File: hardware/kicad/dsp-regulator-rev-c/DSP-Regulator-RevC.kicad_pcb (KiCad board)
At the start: 2 copper layers, 291.9 x 100.9 mm, 218 parts, among them J1 1935161, J10 1935161, J11 1935161, J2 Wire con, J3 Wire con, J4 CLP-110-02-X-D, J5 CLP-110-02-X-D, J8 Conn_01x20_Pin, Q1 BSS138, Q10 PSMN5R2-60YL, Q11 PSMN5R2-60YL, Q12 PSMN5R2-60YL, Q2 BSS138, Q3 BSS138, Q4 BSS138, Q5 PSMN5R2-60YL, Q6 PSMN5R2-60YL, Q7 PSMN5R2-60YL, Q8 PSMN5R2-60YL, Q9 PSMN5R2-60YL, U1 LM2596S-ADJ, U10 INA2180A2IDGKR, U11 TLV1702AIDGKR, U12 TLV1702AIDGKR, U13 INA3221, U14 INA3221, U2 LM2596S-ADJ, U3 LM74502DDFR, U4 TLV9352, U5 TLV9352, U6 LM74502DDFR, U7 LM74502DDFR, U8 LM74502DDFR, U9 INA2180A2IDGKR

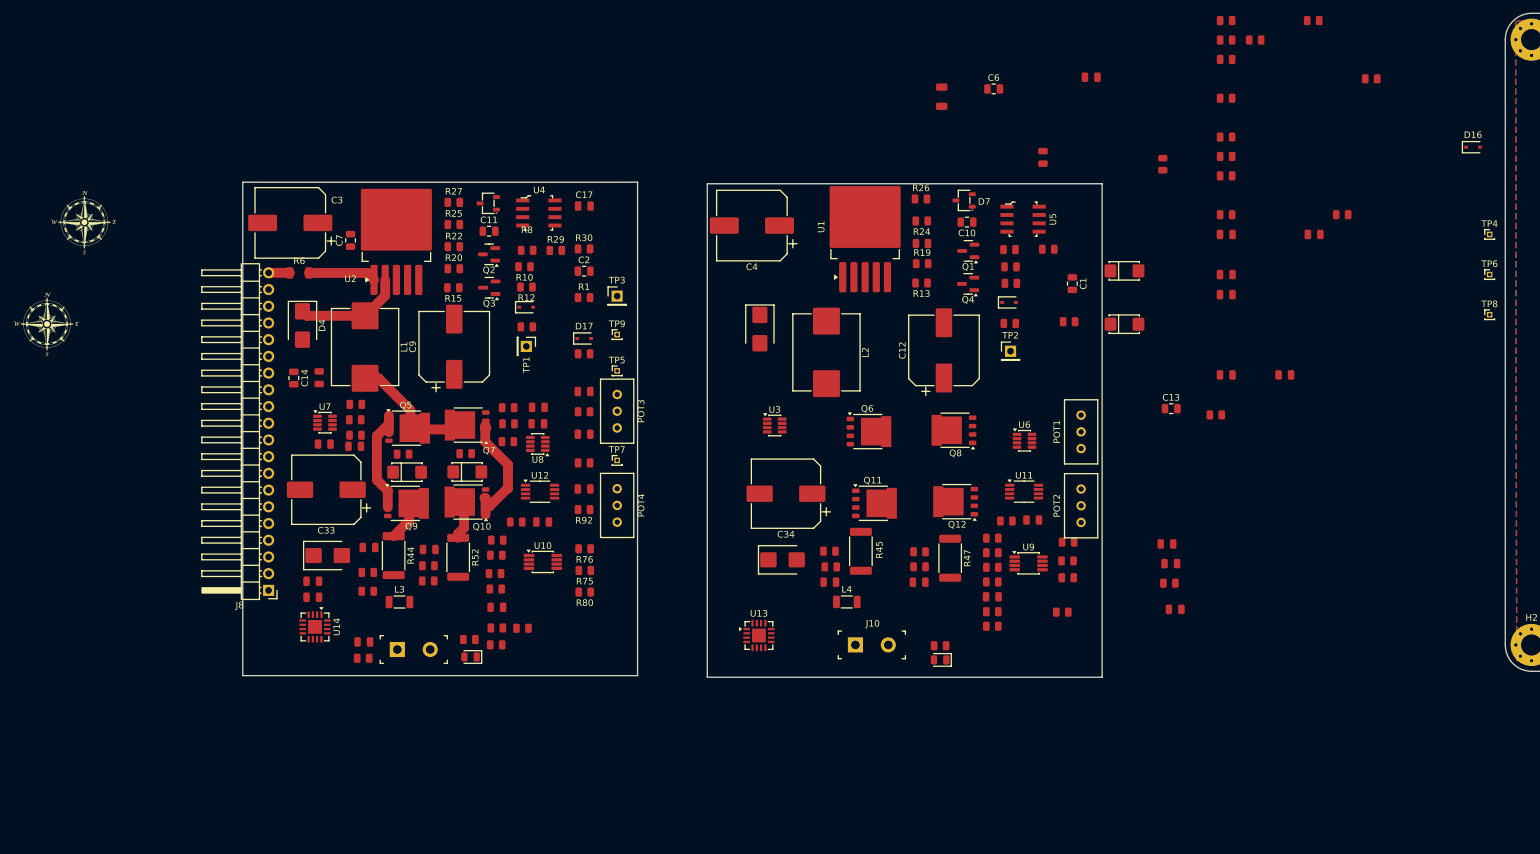
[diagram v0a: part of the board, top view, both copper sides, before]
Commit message: Save Rev-C regulator PCB routing progress
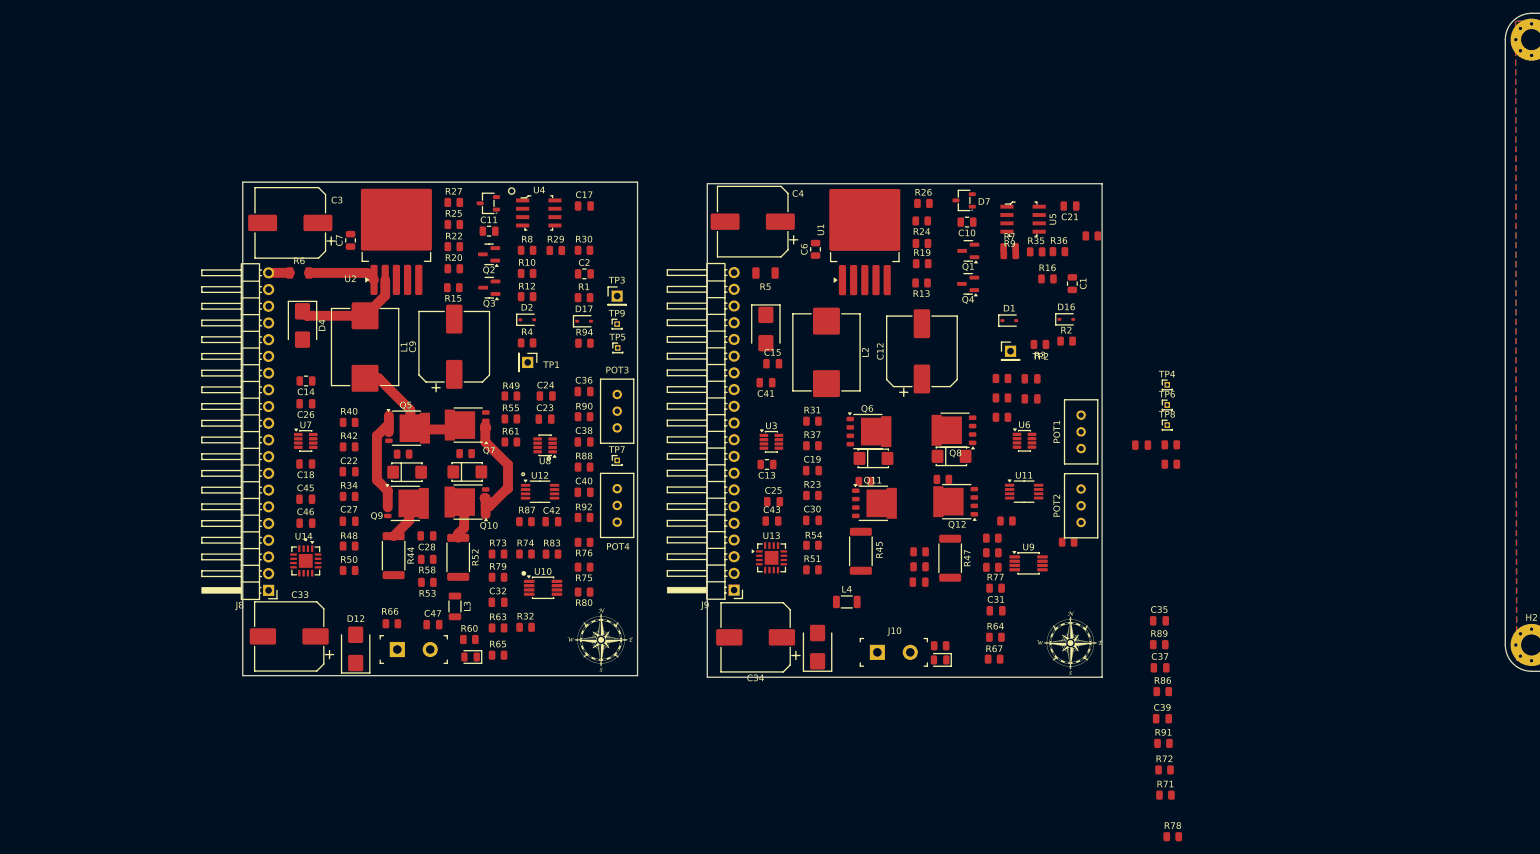
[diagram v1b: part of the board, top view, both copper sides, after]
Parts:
- added J9: Conn_01x20_Pin, Connector_PinHeader_2.54mm:PinHeader_1x20_P2.54mm_Horizontal, F.Cu at (18.3, 144.5)
- moved 10mm1 162.9 mm to (69.5, 152.5)
- moved 10mm2 96.9 mm to (-1.86, 152.0)
- moved R23 95.7 mm to (30.2, 130.1)
- moved R31 83.5 mm to (30.2, 118.8)
- moved R43 81.9 mm to (50.0, 127.7)
- moved C43 81.0 mm to (24.0, 134.0)
- moved R37 78.4 mm to (30.2, 122.6)
- moved C25 71.5 mm to (24.3, 131.1)
- moved R89 71.0 mm to (82.9, 152.8)
- moved C19 69.6 mm to (30.2, 126.3)
- moved R41 68.3 mm to (38.1, 128.0)
- moved R68 68.0 mm to (84.7, 122.4)
- moved D16 67.1 mm to (68.8, 103.3)
- moved R93 66.0 mm to (84.7, 125.4)
- moved C15 65.1 mm to (24.1, 110.1)
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
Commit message: Restore Rev-C regulator PCB updates
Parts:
- removed J10, J11: 1935161, digikey-footprints:Terminal_Block_D1.3mm_P5mm
- removed J8, J9: Conn_01x20_Pin, Connector_PinHeader_2.54mm:PinHeader_1x20_P2.54mm_Horizontal
- removed the TP3 at (233.5, 78.5)
- added C48: 100nF, PCM_JLCPCB:C_0805, F.Cu at (162.9, 160.1)
- added C49: 100nF, PCM_JLCPCB:C_0805, F.Cu at (189.7, 104.2)
- added C50: 1nF, PCM_JLCPCB:C_0805, F.Cu at (162.9, 163.1)
- added C51: 100nF, PCM_JLCPCB:C_0805, F.Cu at (189.7, 107.3)
- added C52: 100nF, PCM_JLCPCB:C_0805, F.Cu at (189.7, 110.3)
- added C53: 100nF, PCM_JLCPCB:C_0805, F.Cu at (189.7, 113.4)
- added D18: SS54B, PCM_JLCPCB:D_SMB, F.Cu at (110.8, 49.9)
- added D19: Yellow, PCM_JLCPCB:D_0805, F.Cu at (124.7, 59.2)
- added D20: 1N5819WS, Diode_SMD:D_SOD-323, F.Cu at (167.3, 163.1)
- added J6: Conn_01x03_Pin, Connector_PinHeader_2.54mm:PinHeader_1x03_P2.54mm_Vertical_SMD_Pin1Right, F.Cu at (158.5, 15.7)
- added J7: Conn_01x06_Pin, Connector_PinHeader_2.54mm:PinHeader_1x06_P2.54mm_Vertical_SMD_Pin1Right, F.Cu at (155.2, 50.6)
- added L5: 33uh, Inductor_SMD:L_Sunlord_MWSA1003S, F.Cu at (112.7, 59.0)
- added R100: 100kΩ, PCM_JLCPCB:R_0805, F.Cu at (185.2, 118.9)
- added R84: 10kΩ, PCM_JLCPCB:R_0805, F.Cu at (149.6, 165.7)
- added R95: 1kΩ, PCM_JLCPCB:R_0805, F.Cu at (158.4, 159.8)
- added R96: 390kΩ, PCM_JLCPCB:R_0805, F.Cu at (185.2, 107.1)
- added R97: 100kΩ, PCM_JLCPCB:R_0805, F.Cu at (185.2, 110.1)
- added R98: 10Ω, PCM_JLCPCB:R_0805, F.Cu at (185.2, 113.0)
- added R99: 390kΩ, PCM_JLCPCB:R_0805, F.Cu at (185.2, 116.0)
- added U15: LM74502DDFR, Package_TO_SOT_SMD:TSOT-23-8, F.Cu at (194.5, 105.1)
- added U16: LM74502DDFR, Package_TO_SOT_SMD:TSOT-23-8, F.Cu at (194.5, 109.7)
- C1: value 1nF -> 100nF; footprint Capacitor_SMD:C_0805_2012Metric -> PCM_JLCPCB:C_0805
- C10: value 100pF -> 10uF; footprint Capacitor_SMD:C_0805_2012Metric -> PCM_JLCPCB:C_0805
- C11: value 100pF -> 100nF; footprint Capacitor_SMD:C_0805_2012Metric -> PCM_JLCPCB:C_0805
- C12, C9: value 330uF 25v -> 100nF; footprint Capacitor_SMD:CP_Elec_10x10.5 -> PCM_JLCPCB:C_0805
- C13, C27, C42: value 100nF -> 1nF
- C14: value 100nF -> 100pF
- C17: value 100nF -> 470uf 50v; footprint PCM_JLCPCB:C_0805 -> Capacitor_SMD:CP_Elec_10x10.5
- C18, C20: footprint PCM_JLCPCB:C_0805 -> Capacitor_SMD:C_0805_2012Metric
- C19: value 100nF -> 330uF 25v; footprint PCM_JLCPCB:C_0805 -> Capacitor_SMD:CP_Elec_10x10.5
- C2: value 1nF -> 100pF
- C21, C23: value 100nF -> 10uF
- C22: value 100nF -> 470uf; footprint PCM_JLCPCB:C_0805 -> Capacitor_SMD:CP_Elec_10x10
- C25: value 10uF -> 1nF; footprint PCM_JLCPCB:C_0805 -> Capacitor_SMD:C_0805_2012Metric
- C26: value 10uF -> 100pF
- C28: value 100nF -> 100nf; footprint PCM_JLCPCB:C_0805 -> Capacitor_SMD:C_0805_2012Metric
- C29: value 100nF -> 1000uf 25v; footprint PCM_JLCPCB:C_0805 -> Capacitor_SMD:C_Elec_10x10.2
- C3: value 470uf 50v -> 100nF; footprint Capacitor_SMD:CP_Elec_10x10.5 -> PCM_JLCPCB:C_0805
- C30: value 100nF -> 470uf 25V; footprint PCM_JLCPCB:C_0805 -> Capacitor_SMD:CP_Elec_10x10.5
- C31: value 10uF -> 100nF
- C32: value 10uF -> 330uF 25v; footprint PCM_JLCPCB:C_0805 -> Capacitor_SMD:CP_Elec_10x10.5
- C33, C34: value 470uf -> 100nF; footprint Capacitor_SMD:CP_Elec_10x10 -> PCM_JLCPCB:C_0805
- C35, C36: value 1nF -> 100nF
- C38: value 1nF -> 100nF; footprint PCM_JLCPCB:C_0805 -> Capacitor_SMD:C_0805_2012Metric
- C5: value 100nf -> 100nF
- C6: value 100nF -> 470uf; footprint Capacitor_SMD:C_0805_2012Metric -> Capacitor_SMD:CP_Elec_10x10
- C7: value 100nF -> 10uF; footprint Capacitor_SMD:C_0805_2012Metric -> PCM_JLCPCB:C_0805
- C8: value 1000uf 25v -> 330uF 25v; footprint Capacitor_SMD:C_Elec_10x10.2 -> Capacitor_SMD:CP_Elec_10x10.5
- D1: value 1N5819WS -> BAT54C,215; footprint PCM_JLCPCB:D_SOD-323 -> PCM_JLCPCB:SOT-23-3_L2.9-W1.6-P1.90-LS2.8-BR
- D10: value 1SMA4742A -> SS54B; footprint PCM_JLCPCB:D_DO-214AC(SMA) -> PCM_JLCPCB:D_SMB
- D11: value 1SMA4742A -> SMBJ6.0CA; footprint PCM_JLCPCB:D_DO-214AC(SMA) -> PCM_JLCPCB:D_SMB
- D12: value SMBJ6.0CA -> Green; footprint PCM_JLCPCB:D_SMB -> PCM_JLCPCB:D_0805
- D13: value SMBJ6.0CA -> 1SMA4742A; footprint PCM_JLCPCB:D_SMB -> PCM_JLCPCB:D_DO-214AC(SMA)
- D14: value Green -> 1N5819WS; footprint PCM_JLCPCB:D_0805 -> PCM_JLCPCB:D_SOD-323
- D15: value Green -> Yellow
- D16: value 1N5819WS -> Red; footprint Diode_SMD:D_SOD-323 -> PCM_JLCPCB:D_0805
- D2: value 1N5819WS -> 1SMA4742A; footprint PCM_JLCPCB:D_SOD-323 -> PCM_JLCPCB:D_DO-214AC(SMA)
- D3: value Red -> SMBJ6.0CA; footprint PCM_JLCPCB:D_0805 -> PCM_JLCPCB:D_SMB
- D4: value SS54B -> Green; footprint PCM_JLCPCB:D_SMB -> PCM_JLCPCB:D_0805
- D6: value BAT54C,215 -> 1SMA4742A; footprint PCM_JLCPCB:SOT-23-3_L2.9-W1.6-P1.90-LS2.8-BR -> PCM_JLCPCB:D_DO-214AC(SMA)
- D7: value BAT54C,215 -> 1N5819WS; footprint PCM_JLCPCB:SOT-23-3_L2.9-W1.6-P1.90-LS2.8-BR -> PCM_JLCPCB:D_SOD-323
- D8: value 1SMA4742A -> BAT54C,215; footprint PCM_JLCPCB:D_DO-214AC(SMA) -> PCM_JLCPCB:SOT-23-3_L2.9-W1.6-P1.90-LS2.8-BR
- J2: value Wire con -> 1935161; footprint Connector_Wire:SolderWire-1sqmm_1x01_D1.4mm_OD2.7mm -> digikey-footprints:Terminal_Block_D1.3mm_P5mm
- J4: value CLP-110-02-X-D -> 1935161; footprint 1My_Parts_ Connectors:SAMTEC_CLP-110-02-X-D -> digikey-footprints:Terminal_Block_D1.3mm_P5mm
- J5: value CLP-110-02-X-D -> Wire con; footprint 1My_Parts_ Connectors:SAMTEC_CLP-110-02-X-D -> Connector_Wire:SolderWire-1sqmm_1x01_D1.4mm_OD2.7mm
- L1: value 33uh -> L_Ferrite; footprint Inductor_SMD:L_Sunlord_MWSA1003S -> Inductor_SMD:L_1206_3216Metric
- L3: value L_Ferrite -> 33uh; footprint Inductor_SMD:L_1206_3216Metric -> Inductor_SMD:L_Sunlord_MWSA1003S
- Q1, Q2, Q4: value BSS138 -> PSMN5R2-60YL; footprint PCM_JLCPCB:Q_SOT-23 -> Package_TO_SOT_SMD:LFPAK56
- Q12, Q6, Q9: value PSMN5R2-60YL -> BSS138; footprint Package_TO_SOT_SMD:LFPAK56 -> PCM_JLCPCB:Q_SOT-23
- R10: value 100kΩ -> 100Ω
- R11: value 1kΩ -> 0Ω; footprint PCM_JLCPCB:R_0805 -> PCM_JLCPCB:R_1206
- R12, R41, R46: value 100kΩ -> 10Ω
- R13: value 10kΩ -> 33kΩ
- R14, R58, R63: value 10Ω -> 10kΩ
- R15, R75, R92: value 10kΩ -> 10Ω
- R16: value 100kΩ -> 270Ω
- R17: value 10mohm -> 10Ω
- R18: value 10Ω -> 100Ω
- R19: value 1kΩ -> 200mΩ; footprint PCM_JLCPCB:R_0805 -> Resistor_SMD:R_2512_6332Metric
- R2: value 100Ω -> 1kΩ
- R20: value 1kΩ -> 10Ω
- R21: value 100Ω -> 100kΩ
- R22: value 680Ω -> 100kΩ
- R24: value 1kΩ -> 47kΩ
- R25: value 820Ω -> 100Ω
- R26: value 1.8kΩ -> 100kΩ
- R27: value 0Ω -> 100kΩ
- R28, R57: value 10Ω -> 1kΩ
- R29: value 1kΩ -> 33kΩ
- R3: value 47kΩ -> 1.8kΩ
- R30: value 33kΩ -> 680Ω
- R31: value 390kΩ -> 820Ω
- R32: value 100kΩ -> 0Ω
- R33, R56: value 100kΩ -> 1kΩ
- R35: value 100Ω -> 0Ω; footprint PCM_JLCPCB:R_0805 -> PCM_JLCPCB:R_1206
- R36: value 33kΩ -> 100kΩ
- R37: value 100kΩ -> 20m ohms; footprint PCM_JLCPCB:R_0805 -> Resistor_SMD:R_2512_6332Metric
- R38, R40: value 390kΩ -> 10Ω
- R39, R42, R43: value 100kΩ -> 10kΩ
- R4: value 47kΩ -> 10Ω
- R44: value 20m ohms -> 100Ω; footprint Resistor_SMD:R_2512_6332Metric -> PCM_JLCPCB:R_0805
- R45: value 20mΩ -> 200m ohms
- R47: value 200mΩ -> 270Ω; footprint Resistor_SMD:R_2512_6332Metric -> PCM_JLCPCB:R_0805
- R48, R49, R53: value 10Ω -> 100kΩ
- R5: value 0Ω -> 1kΩ; footprint PCM_JLCPCB:R_1206 -> PCM_JLCPCB:R_0805
- R50: value 10Ω -> 47kΩ
- R52: value 200m ohms -> 100Ω; footprint Resistor_SMD:R_2512_6332Metric -> PCM_JLCPCB:R_0805
- R54: value 10Ω -> 270Ω
- R55: value 390kΩ -> 100kΩ
- R6: value 0Ω -> 100kΩ; footprint PCM_JLCPCB:R_1206 -> PCM_JLCPCB:R_0805
- R60: value 270Ω -> 10Ω
- R61: value 100kΩ -> 3100
- R62: value 270Ω -> 10kΩ
- R64: value 10Ω -> 10mohm
- R65: value 10Ω -> 1k
- R66, R67: value 10Ω -> 510kΩ
- R68: value 10Ω -> 0Ω; footprint PCM_JLCPCB:R_0805 -> PCM_JLCPCB:R_1206
- R69: value 10kΩ -> 680Ω
- R7: value 100Ω -> 20mΩ; footprint PCM_JLCPCB:R_0805 -> Resistor_SMD:R_2512_6332Metric
- R73, R74: value 10kΩ -> 510kΩ
- R76: value 10kΩ -> 1kΩ
- R77: value 510kΩ -> 390kΩ
- R78, R79: value 510kΩ -> 100kΩ
- R8: value 100Ω -> 10Ω
- R80: value 510kΩ -> 1kΩ
- R81, R83: value 510kΩ -> 10kΩ
- R82: value 510kΩ -> 10Ω
- R85: value 1kΩ -> 390kΩ
- R86, R87: value 1kΩ -> 510kΩ
- R88: value 1kΩ -> 100kΩ
- R93, R94: value 100kΩ -> 510kΩ
- U1: value LM2596S-ADJ -> TLV9352; footprint Package_TO_SOT_SMD:TO-263-5_TabPin3 -> digikey-footprints:SOIC-8_W3.9mm
- U10: value INA2180A2IDGKR -> INA3221; footprint Package_SO:VSSOP-8_3x3mm_P0.65mm -> Package_DFN_QFN:Texas_RGV0016A_VQFN-16-1EP_4x4mm_P0.65mm_EP2.1x2.1mm
- U11: value TLV1702AIDGKR -> INA3221; footprint Package_SO:Texas_S-PDSO-G8_3x3mm_P0.65mm -> Package_DFN_QFN:Texas_RGV0016A_VQFN-16-1EP_4x4mm_P0.65mm_EP2.1x2.1mm
- U12: value TLV1702AIDGKR -> INA2180A2IDGKR; footprint Package_SO:Texas_S-PDSO-G8_3x3mm_P0.65mm -> Package_SO:VSSOP-8_3x3mm_P0.65mm
- U13: value INA3221 -> TLV1702AIDGKR; footprint Package_DFN_QFN:Texas_RGV0016A_VQFN-16-1EP_4x4mm_P0.65mm_EP2.1x2.1mm -> Package_SO:Texas_S-PDSO-G8_3x3mm_P0.65mm
- U14: value INA3221 -> LM74502DDFR; footprint Package_DFN_QFN:Texas_RGV0016A_VQFN-16-1EP_4x4mm_P0.65mm_EP2.1x2.1mm -> Package_TO_SOT_SMD:TSOT-23-8
- U3: value LM74502DDFR -> TLV9352; footprint Package_TO_SOT_SMD:TSOT-23-8 -> digikey-footprints:SOIC-8_W3.9mm
- U4: value TLV9352 -> LM2596S-ADJ; footprint digikey-footprints:SOIC-8_W3.9mm -> Package_TO_SOT_SMD:TO-263-5_TabPin3
- U5: value TLV9352 -> AW9523B; footprint digikey-footprints:SOIC-8_W3.9mm -> Package_DFN_QFN:QFN-24-1EP_4x4mm_P0.5mm_EP2.7x2.7mm
- U6: value LM74502DDFR -> INA2180A2IDGKR; footprint Package_TO_SOT_SMD:TSOT-23-8 -> Package_SO:VSSOP-8_3x3mm_P0.65mm
- U7: value LM74502DDFR -> TLV1702AIDGKR; footprint Package_TO_SOT_SMD:TSOT-23-8 -> Package_SO:Texas_S-PDSO-G8_3x3mm_P0.65mm
- U8: value LM74502DDFR -> LM2596S-ADJ; footprint Package_TO_SOT_SMD:TSOT-23-8 -> Package_TO_SOT_SMD:TO-263-5_TabPin3
- U9: value INA2180A2IDGKR -> LM74502DDFR; footprint Package_SO:VSSOP-8_3x3mm_P0.65mm -> Package_TO_SOT_SMD:TSOT-23-8
- moved U7 310.3 mm to (259.7, 170.2)
- moved C27 299.7 mm to (258.7, 154.6), turned to 0 degrees
- moved R50 289.8 mm to (237.7, 59.6), turned to 0 degrees
- moved R48 289.5 mm to (237.7, 56.7), turned to 0 degrees
- moved R53 286.6 mm to (247.4, 65.1)
- moved Q9 285.4 mm to (242.4, 51.7)
- moved D14 284.7 mm to (246.7, 60.0), turned to 0 degrees
- moved R44 284.3 mm to (237.7, 53.7), turned to 0 degrees
- moved R66 283.7 mm to (249.9, 154.5), turned to 0 degrees
- moved C18 278.2 mm to (224.2, 62.6), turned to 0 degrees
- moved R58 274.6 mm to (245.5, 160.4), turned to 0 degrees
- moved D17 274.3 mm to (263.1, 163.7)
- moved D12 274.0 mm to (234.6, 144.9), turned to 0 degrees
- moved C14 273.0 mm to (214.8, 34.7), turned to -90 degrees
- moved R52 272.5 mm to (237.7, 62.6), turned to 0 degrees
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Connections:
- C1 pad 1: Net-(C1-Pad1) -> +12V
- C10 pad 1: Net-(D7-K) -> +5V_reg
- C10 pad 2: Net-(U1-FB) -> GND
- C11 pad 1: Net-(D6-K) -> Net-(C11-Pad1)
- C11 pad 2: Net-(U2-FB) -> Net-(Q5-D)
- C12 pad 1: +5V_reg -> +12V
- C13 pad 1: +5V_Boot -> Net-(C13-Pad1)
- C13 pad 2: Net-(U3-VCAP) -> GND
- C14 pad 1: +3.3V_Reg -> Ref_3.3V
- C14 pad 2: GND -> Net-(U4-FB)
- C15 pad 1: +5V_reg -> +3.3V Boot
- C15 pad 2: GND -> unconnected-(C15-Pad2)
- C16 pad 1: +5V_Boot -> Net-(Q8-D)
- C16 pad 2: Net-(U6-VCAP) -> Net-(C16-Pad2)
- C17 pad 1: +12V -> Net-(U4-VIN)
- C18 pad 1: +5V_Boot -> Net-(U4-VIN)
- C18 pad 2: Net-(U7-VCAP) -> GND
- C19 pad 1: GND -> +3.3V_Reg
- C19 pad 2: +5V_Boot -> GND
- C2 pad 1: Net-(C2-Pad1) -> Ref_5V
- C2 pad 2: GND -> Net-(U2-FB)
- C20 pad 1: GND -> +3.3V_Reg
- C20 pad 2: +5V_Boot -> GND
- C21 pad 1: +12V -> +3.3V_Reg
- C22 pad 1: GND -> Net-(C16-Pad2)
- C22 pad 2: +5V_Boot -> GND
- C23 pad 1: +5V_Boot -> Net-(C16-Pad2)
- C23 pad 2: Net-(U8-VCAP) -> GND
- C24 pad 1: GND -> Net-(C16-Pad2)
- C24 pad 2: +5V_Boot -> Net-(Q11-D)
- C25 pad 1: +5V_reg -> Net-(C25-Pad1)
- C26 pad 1: +3.3V_Reg -> +5V_Boot
- C26 pad 2: GND -> Net-(U8-FB)
- C27 pad 1: Net-(Q9-D) -> Net-(U7A-IN-)
- C27 pad 2: Net-(C27-Pad2) -> Net-(U7A-IN+)
- C28 pad 1: Net-(C27-Pad2) -> Net-(C28-Pad1)
- C28 pad 2: Net-(Q10-D) -> GND
- C29 pad 1: Shunt - -> Net-(C28-Pad1)
- C29 pad 2: Net-(Q12-D) -> GND
- C3 pad 1: Net-(U2-VIN) -> Net-(Q2-D)
- C3 pad 2: GND -> Net-(C11-Pad1)
- C30 pad 1: Net-(Q11-D) -> Net-(U8-VIN)
- C30 pad 2: Shunt - -> GND
- C31 pad 1: Shunt - -> Net-(U8-VIN)
- C32 pad 1: Net-(C27-Pad2) -> +5V_Boot
- C33 pad 1: Net-(C27-Pad2) -> +5V_Boot
- C34 pad 1: Shunt - -> +12V
- C35 pad 1: Net-(U11A-IN-) -> +3.3V Boot
- C35 pad 2: Net-(U11A-IN+) -> GND
- C36 pad 1: Net-(U12A-IN-) -> GND
- C36 pad 2: Net-(U12A-IN+) -> +5V_Boot
- C37 pad 1: Net-(U11B-IN-) -> Net-(U7B-IN-)
- C37 pad 2: Net-(U11B-IN+) -> Net-(U7B-IN+)
- C38 pad 1: Net-(U12B-IN-) -> +5V_Boot
- C38 pad 2: Net-(U12B-IN+) -> Net-(U9-VCAP)
- C39 pad 1: +12V -> +3.3V Boot
- C4 pad 1: Net-(U1-VIN) -> Net-(U2-VIN)
- C40 pad 1: +12V -> +3.3V Boot
- C41 pad 1: +3.3V Boot -> GND
- C41 pad 2: GND -> +5V_Boot
- C42 pad 1: +3.3V Boot -> Net-(U13A-IN-)
- C42 pad 2: GND -> Net-(U13A-IN+)
- C43 pad 1: +3.3V Boot -> Net-(U10-TC)
- C44 pad 1: Net-(U13-TC) -> Net-(U11-TC)
- C45 pad 1: Incoming (+) -> +5V_Boot
- C45 pad 2: Incoming (-) -> Net-(U14-VCAP)
- C46 pad 1: +3.3V Boot -> Incoming (+)
- C46 pad 2: GND -> Incoming (-)
- C47 pad 1: Net-(U14-TC) -> +12V
- C5 pad 1: Net-(C5-Pad1) -> Net-(U2-VIN)
- C6 pad 1: Net-(U1-VIN) -> Net-(C11-Pad1)
- C7 pad 1: Net-(U2-VIN) -> Net-(C11-Pad1)
- C8 pad 1: Net-(C5-Pad1) -> +5V_reg
- C9 pad 1: +3.3V_Reg -> +5V_reg
- D1 pad 1: Net-(Q4-G) -> Net-(D1-A-Pad1)
- D1 pad 2: Net-(C1-Pad1) -> Net-(D1-A-Pad2)
- D10 pad 1: SRC 3.3_LOW -> Net-(U4-OUT)
- D10 pad 2: Gate _3.3_LOW -> GND
- D11 pad 1: SRC 5_LOW -> GND
- D11 pad 2: Gate _5_LOW -> Net-(C16-Pad2)
- D12 pad 1: GND -> Net-(D12-Pad1)
- D12 pad 2: Net-(C27-Pad2) -> V_out +3V3
- D13 pad 1: GND -> SRC 3.3_LOW
- D13 pad 2: Shunt - -> Gate _3.3_LOW
- D14 pad 1: Net-(D14-Pad1) -> Net-(Q12-G)
- D14 pad 2: V_out +3V3 -> Net-(C25-Pad1)
- D15 pad 2: V_out +5V -> Net-(U5-P1_0)
- D16 pad 1: FAULT_CRITICAL_SUM -> Net-(D16-Pad1)
- D16 pad 2: Net-(D16-A) -> Net-(C28-Pad1)
- D2 pad 1: Net-(Q3-G) -> SRC 5_HIGH
- D2 pad 2: Net-(C2-Pad1) -> Gate _5_High
- D3 pad 1: Net-(D3-Pad1) -> GND
- D3 pad 2: Net-(C5-Pad1) -> Net-(C11-Pad1)
- D4 pad 1: Net-(U2-OUT) -> Net-(D4-Pad1)
- D4 pad 2: GND -> V_out +5V
- D5 pad 1: Net-(U1-OUT) -> Net-(U2-OUT)
- D6 pad 1: Net-(D6-A-Pad1) -> SRC 5_LOW
- D6 pad 2: Net-(D6-A-Pad2) -> Gate _5_LOW
- D7 pad 1: Net-(D7-A-Pad1) -> Net-(Q6-G)
- D7 pad 2: Net-(D7-A-Pad2) -> Net-(C13-Pad1)
- D8 pad 1: SRC 3.3_HIGH -> Net-(D8-A-Pad1)
- D8 pad 2: Gate _3.3_HIGH -> Net-(D8-A-Pad2)
- D9 pad 1: SRC 5_HIGH -> SRC 3.3_HIGH
- D9 pad 2: Gate _5_High -> Gate _3.3_HIGH
- F1 pad 1: Net-(J2-Pin_1) -> Net-(J3-Pin_1)
- J1 pad 1: Net-(J2-Pin_1) -> GND
- J1 pad 2: GND -> V_out +5V
- J2 pad 1: Net-(J2-Pin_1) -> GND
- J3 pad 1: GND -> Net-(J3-Pin_1)
- L1 pad 1: Net-(U2-OUT) -> Net-(C11-Pad1)
- L1 pad 2: +3.3V_Reg -> V_out +5V
- L2 pad 1: Net-(U1-OUT) -> Net-(U2-OUT)
- L3 pad 1: Net-(C27-Pad2) -> Net-(U4-OUT)
- L3 pad 2: V_out +3V3 -> +3.3V_Reg
- L4 pad 1: Shunt - -> Net-(C16-Pad2)
- L4 pad 2: V_out +5V -> V_out +3V3
- Q1 pad 1: Net-(Q1-G) -> SRC 5_HIGH
- Q1 pad 2: GND -> SRC 5_HIGH
- Q1 pad 3: Net-(Q1-D) -> SRC 5_HIGH
- Q10 pad 5: Net-(Q10-D) -> +3.3V_Reg
- Q11 pad 1: SRC 5_HIGH -> SRC 3.3_LOW
- Q11 pad 2: SRC 5_HIGH -> SRC 3.3_LOW
- Q11 pad 3: SRC 5_HIGH -> SRC 3.3_LOW
- Q11 pad 4: Gate _5_High -> Gate _3.3_LOW
- Q12 pad 1: SRC 5_LOW -> Net-(Q12-G)
- Q12 pad 2: SRC 5_LOW -> GND
- Q12 pad 3: SRC 5_LOW -> Net-(Q12-D)
- Q2 pad 1: Net-(Q2-G) -> SRC 5_HIGH
- Q2 pad 2: GND -> SRC 5_HIGH
- Q2 pad 3: Net-(Q2-D) -> SRC 5_HIGH
- Q3 pad 3: Net-(Q2-D) -> Net-(Q3-D)
- Q4 pad 1: Net-(Q4-G) -> SRC 5_LOW
- Q4 pad 2: GND -> SRC 5_LOW
- Q4 pad 3: Net-(Q1-D) -> SRC 5_LOW
- Q5 pad 1: SRC 3.3_HIGH -> SRC 5_LOW
- Q5 pad 2: SRC 3.3_HIGH -> SRC 5_LOW
- Q5 pad 3: SRC 3.3_HIGH -> SRC 5_LOW
- Q5 pad 4: Gate _3.3_HIGH -> Gate _5_LOW
- Q5 pad 5: +3.3V_Reg -> Net-(Q5-D)
- Q6 pad 1: SRC 5_HIGH -> Net-(Q6-G)
- Q6 pad 2: SRC 5_HIGH -> GND
- Q6 pad 3: SRC 5_HIGH -> Net-(Q3-D)
- Q7 pad 1: SRC 3.3_LOW -> SRC 3.3_HIGH
- Q7 pad 2: SRC 3.3_LOW -> SRC 3.3_HIGH
- Q7 pad 3: SRC 3.3_LOW -> SRC 3.3_HIGH
- Q7 pad 4: Gate _3.3_LOW -> Gate _3.3_HIGH
- Q8 pad 1: SRC 5_LOW -> SRC 3.3_HIGH
- Q8 pad 2: SRC 5_LOW -> SRC 3.3_HIGH
- Q8 pad 3: SRC 5_LOW -> SRC 3.3_HIGH
- Q8 pad 4: Gate _5_LOW -> Gate _3.3_HIGH
- Q8 pad 5: +5V_reg -> Net-(Q8-D)
- Q9 pad 1: SRC 3.3_HIGH -> Net-(Q9-G)
- Q9 pad 2: SRC 3.3_HIGH -> GND
- Q9 pad 3: SRC 3.3_HIGH -> Net-(Q12-D)
- R1 pad 1: FAULT_CRITICAL_SUM -> Net-(U2-FB)
- R1 pad 2: Net-(C2-Pad1) -> Net-(R1-Pad2)
- R10 pad 1: GND -> +5V_reg
- R10 pad 2: Net-(Q2-G) -> Net-(R10-Pad2)
- R11 pad 1: Net-(D3-Pad1) -> +12V
- R11 pad 2: GND -> Net-(U2-VIN)
- R12 pad 1: GND -> V_out +5V
- R12 pad 2: Net-(Q3-G) -> VSENSE_5V+
- R13 pad 1: +5V_Boot -> Net-(R10-Pad2)
- R13 pad 2: Net-(Q1-D) -> GND
- R14 pad 1: Incoming (+) -> +5V_Boot
- R14 pad 2: Net-(C5-Pad1) -> Net-(Q3-D)
- R15 pad 1: +5V_Boot -> Net-(C11-Pad1)
- R15 pad 2: Net-(Q2-D) -> VSENSE_5V+
- R16 pad 1: GND -> Net-(D4-Pad1)
- R16 pad 2: Net-(Q4-G) -> GND
- R17 pad 1: Net-(C5-Pad1) -> GND
- R17 pad 2: +12V -> VSENSE_5V-
- R18 pad 1: Incoming (-) -> ISET_MPU_5V
- R18 pad 2: +12V -> Net-(Q3-G)
- R19 pad 1: Net-(U1-FB) -> Net-(Q5-D)
- R19 pad 2: GND -> Net-(C11-Pad1)
- R2 pad 1: FAULT_CRITICAL_SUM -> Net-(R1-Pad2)
- R2 pad 2: Net-(C1-Pad1) -> Net-(R2-Pad2)
- R20 pad 1: Net-(U2-FB) -> Net-(C11-Pad1)
- R20 pad 2: GND -> -5V_low_Range
- R21 pad 1: Net-(U1-FB) -> GND
- R21 pad 2: Net-(R21-Pad2) -> Net-(Q3-G)
- R22 pad 1: Net-(U2-FB) -> SRC 5_LOW
- R22 pad 2: Net-(R22-Pad2) -> Gate _5_LOW
- R23 pad 1: Net-(U3-GATE) -> Net-(Q5-D)
- R23 pad 2: Gate _5_High -> +5V_low_Range
- R24 pad 1: Net-(R21-Pad2) -> +5V_Boot
- R24 pad 2: Net-(R24-Pad2) -> Net-(C13-Pad1)
- R25 pad 1: Net-(R22-Pad2) -> FAULT_CRITICAL_SUM
- R25 pad 2: Net-(R25-Pad2) -> Net-(C13-Pad1)
- R26 pad 1: Net-(R24-Pad2) -> GND
- R26 pad 2: Net-(D7-K) -> Net-(Q6-G)
- R27 pad 1: Net-(R25-Pad2) -> VSENSE_3V3+
- R27 pad 2: Net-(D6-K) -> GND
- R28 pad 1: Net-(U6-GATE) -> +3.3V_Reg
- R28 pad 2: Gate _5_LOW -> Net-(R28-Pad2)
- R29 pad 1: +3.3V_Reg -> Net-(R28-Pad2)
- R29 pad 2: Net-(R29-Pad2) -> GND
- R3 pad 1: +5V_Boot -> Net-(R2-Pad2)
- R3 pad 2: Net-(C1-Pad1) -> Ref_5V
- R30 pad 1: Net-(R29-Pad2) -> Net-(U4-FB)
- R30 pad 2: GND -> Net-(R30-Pad2)
- R31 pad 1: +5V_Boot -> Net-(R30-Pad2)
- R31 pad 2: Net-(U3-OV) -> Net-(R31-Pad2)
- R32 pad 1: VSENSE_3V3+ -> Net-(R31-Pad2)
- R32 pad 2: GND -> Ref_3.3V
- R33 pad 1: VSENSE_5V+ -> Net-(U4-FB)
- R34 pad 1: Net-(U7-GATE) -> Net-(Q8-D)
- R34 pad 2: Gate _3.3_HIGH -> +3v3V_Hi_Range 
- R35 pad 1: +5V_reg -> +12V
- R35 pad 2: Net-(R35-Pad2) -> Net-(U4-VIN)
- R36 pad 1: Net-(R35-Pad2) -> SRC 3.3_HIGH
- R36 pad 2: GND -> Gate _3.3_HIGH
- R37 pad 1: Net-(U3-OV) -> Net-(Q8-D)
- R37 pad 2: GND -> Net-(C16-Pad2)
- R38 pad 1: +5V_Boot -> Net-(C16-Pad2)
- R38 pad 2: Net-(U6-OV) -> -3v3V_Hi_Range
- R39 pad 1: Net-(U6-OV) -> +5V_Boot
- R39 pad 2: GND -> Net-(Q12-D)
- R4 pad 1: +5V_Boot -> Net-(Q2-D)
- R4 pad 2: Net-(C2-Pad1) -> +5V_Hi_Range 
- R40 pad 1: +5V_Boot -> Net-(C16-Pad2)
- R40 pad 2: Net-(U7-OV) -> VSENSE_3V3+
- R41 pad 1: SRC 5_HIGH -> V_out +3V3
- R41 pad 2: Gate _5_High -> VSENSE_3V3+
- R42 pad 1: Net-(U7-OV) -> Net-(U5-~{RST})
- R42 pad 2: GND -> +3.3V Boot
- R43 pad 1: SRC 5_LOW -> Net-(U5-~{INT})
- R43 pad 2: Gate _5_LOW -> +3.3V Boot
- R44 pad 1: Net-(Q9-D) -> ISET_MPU_3V3
- R44 pad 2: Net-(C27-Pad2) -> Net-(Q9-G)
- R45 pad 2: Shunt - -> Net-(C16-Pad2)
- R46 pad 1: SRC 3.3_HIGH -> Net-(C16-Pad2)
- R46 pad 2: Gate _3.3_HIGH -> -3v3V_low_Range
- R47 pad 1: Net-(Q12-D) -> Net-(D12-Pad1)
- R47 pad 2: Shunt - -> GND
- R48 pad 1: Net-(Q9-D) -> GND
- R48 pad 2: +3v3V_Hi_Range  -> Net-(Q9-G)
- R49 pad 1: Net-(U8-GATE) -> SRC 3.3_LOW
- R5 pad 1: +12V -> Net-(U2-FB)
- R5 pad 2: Net-(U1-VIN) -> GND
- R50 pad 1: Net-(C27-Pad2) -> +5V_Boot
- R50 pad 2: -3v3V_Hi_Range -> Net-(C25-Pad1)
- R51 pad 2: +5V_Hi_Range  -> +3v3V_low_Range
- R52 pad 1: Net-(Q10-D) -> FAULT_CRITICAL_SUM
- R52 pad 2: Net-(C27-Pad2) -> Net-(C25-Pad1)
- R53 pad 1: Net-(C27-Pad2) -> GND
- R53 pad 2: -3v3V_low_Range -> Net-(Q12-G)
- R54 pad 1: Shunt - -> Net-(D15-Pad1)
- R54 pad 2: -5V_Hi_Range -> GND
- R55 pad 1: +5V_Boot -> +3.3V Boot
- R55 pad 2: Net-(U8-OV) -> Net-(D17-A)
- R56 pad 1: SRC 3.3_LOW -> Net-(U7A-IN+)
- R56 pad 2: Gate _3.3_LOW -> Net-(R56-Pad2)
- R57 pad 1: Shunt - -> Net-(D16-Pad1)
- R57 pad 2: -5V_low_Range -> GND
- R58 pad 1: Net-(Q10-D) -> +3v3V_Hi_Range 
- R58 pad 2: +3v3V_low_Range -> Net-(U6A-+)
- R59 pad 1: Net-(Q12-D) -> Incoming (+)
- R59 pad 2: +5V_low_Range -> Net-(C28-Pad1)
- R6 pad 1: +12V -> VSENSE_5V+
- R6 pad 2: Net-(U2-VIN) -> GND
- R60 pad 1: Net-(D14-Pad1) -> Incoming (-)
- R60 pad 2: GND -> +12V
- R61 pad 1: Net-(U8-OV) -> Net-(U8-FB)
- R61 pad 2: GND -> +5V_Boot
- R62 pad 1: Net-(D15-Pad1) -> -3v3V_Hi_Range
- R62 pad 2: GND -> Net-(U6A--)
- R63 pad 1: Net-(C27-Pad2) -> Net-(POT1-Pad2)
- R63 pad 2: VSENSE_3V3+ -> Net-(U7A-IN-)
- R64 pad 1: Shunt - -> Net-(C28-Pad1)
- R64 pad 2: VSENSE_5V+ -> +12V
- R65 pad 1: V_out +3V3 -> Net-(U8-FB)
- R65 pad 2: VSENSE_3V3+ -> GND
- R66 pad 2: VSENSE_3V3- -> Net-(U6A-+)
- R67 pad 1: V_out +5V -> Net-(U6A--)
- R67 pad 2: VSENSE_5V+ -> Net-(R56-Pad2)
- R68 pad 1: GND -> +12V
- R68 pad 2: VSENSE_5V- -> Net-(U8-VIN)
- R69 pad 1: +5V_Hi_Range  -> GND
- R69 pad 2: Net-(U9A-+) -> Net-(D19-Pad1)
- R7 pad 1: ISET_MPU_5V -> Net-(Q2-D)
- R7 pad 2: Net-(Q1-G) -> Net-(C11-Pad1)
- R70 pad 1: -5V_Hi_Range -> +3v3V_low_Range
- R70 pad 2: Net-(U9A--) -> Net-(U6B-+)
- R71 pad 1: +5V_low_Range -> Net-(POT2-Pad2)
- R71 pad 2: Net-(U9B-+) -> Net-(U7B-IN-)
- R72 pad 1: -5V_low_Range -> -3v3V_low_Range
- R72 pad 2: Net-(U9B--) -> Net-(U6B--)
- R73 pad 1: +3v3V_Hi_Range  -> GND
- R73 pad 2: Net-(U10A-+) -> Net-(U6B-+)
- R74 pad 1: -3v3V_Hi_Range -> Net-(U6B--)
- R74 pad 2: Net-(U10A--) -> Net-(R74-Pad2)
- R75 pad 1: +3v3V_low_Range -> Net-(U9-GATE)
- R75 pad 2: Net-(U10B-+) -> Gate _5_High
- R76 pad 1: -3v3V_low_Range -> Net-(R74-Pad2)
- R76 pad 2: Net-(U10B--) -> Net-(U7B-IN+)
- R77 pad 1: GND -> +5V_Boot
- R77 pad 2: Net-(U9A-+) -> Net-(U9-OV)
- R78 pad 1: GND -> Net-(U9-OV)
- R78 pad 2: Net-(U9B-+) -> GND
- R79 pad 1: GND -> +3.3V Boot
- R79 pad 2: Net-(U10A-+) -> Net-(D20-A)
- R8 pad 1: ISET_MPU_3V3 -> Net-(C11-Pad1)
- R8 pad 2: Net-(Q2-G) -> -5V_Hi_Range
- R80 pad 1: GND -> Net-(U13A-IN+)
- R80 pad 2: Net-(U10B-+) -> Net-(R80-Pad2)
- R81 pad 1: Net-(U9A--) -> +5V_Hi_Range 
- R81 pad 2: Net-(R81-Pad2) -> Net-(U12A-+)
- R82 pad 1: Net-(U9B--) -> Net-(U14-GATE)
- R82 pad 2: Net-(R82-Pad2) -> Gate _5_LOW
- R83 pad 1: Net-(U10A--) -> -5V_Hi_Range
- R83 pad 2: Net-(R83-Pad2) -> Net-(U12A--)
- R85 pad 1: Net-(U11A-IN+) -> +5V_Boot
- R85 pad 2: Net-(R81-Pad2) -> Net-(U14-OV)
- R86 pad 1: Net-(R82-Pad2) -> GND
- R86 pad 2: Net-(U11B-IN+) -> Net-(U12A-+)
- R87 pad 1: Net-(U12A-IN+) -> Net-(U12A--)
- R87 pad 2: Net-(R83-Pad2) -> Net-(R80-Pad2)
- R88 pad 1: Net-(R84-Pad2) -> Net-(U14-OV)
- R88 pad 2: Net-(U12B-IN+) -> GND
- R89 pad 1: Net-(POT1-Pad2) -> +5V_low_Range
- R89 pad 2: Net-(U11A-IN-) -> Net-(U12B-+)
- R9 pad 1: GND -> SRC 5_HIGH
- R9 pad 2: Net-(Q1-G) -> Gate _5_High
- R90 pad 1: Net-(POT3-Pad2) -> Net-(POT4-Pad2)
- R90 pad 2: Net-(U12A-IN-) -> Net-(U13B-IN-)
- R91 pad 1: Net-(POT2-Pad2) -> -5V_low_Range
- R91 pad 2: Net-(U11B-IN-) -> Net-(U12B--)
- R92 pad 1: Net-(POT4-Pad2) -> Net-(U15-GATE)
- R92 pad 2: Net-(U12B-IN-) -> Gate _3.3_HIGH
- R93 pad 1: +3.3V Boot -> GND
- R93 pad 2: Net-(D16-A) -> Net-(U12B-+)
- R94 pad 1: +3.3V Boot -> Net-(U12B--)
- R94 pad 2: Net-(D17-A) -> Net-(R94-Pad2)
- RT1 pad 2: Net-(C5-Pad1) -> Net-(C28-Pad1)
- TP1 pad 1: Net-(Q3-G) -> Net-(Q6-G)
- TP2 pad 1: Net-(Q4-G) -> FAULT_CRITICAL_SUM
- TP3 pad 1: FAULT_CRITICAL_SUM -> Net-(Q12-G)
- TP4 pad 1: Net-(U11A-IN+) -> Net-(U7A-IN+)
- TP5 pad 1: Net-(U12A-IN+) -> Net-(D17-A)
- TP6 pad 1: Net-(U11B-IN+) -> Net-(U7B-IN+)
- TP7 pad 1: Net-(U12B-IN+) -> Net-(U13A-IN+)
- TP8 pad 1: Net-(D16-A) -> Net-(D20-A)
- TP9 pad 1: Net-(D17-A) -> Net-(U13B-IN+)
- U1 pad 1: Net-(U1-VIN) -> Net-(D1-A-Pad1)
- U1 pad 2: Net-(U1-OUT) -> Net-(D1-A-Pad1)
- U1 pad 3: GND -> VSENSE_5V+
- U1 pad 4: Net-(U1-FB) -> GND
- U1 pad 5: Net-(Q1-D) -> Net-(R10-Pad2)
- U10 pad 1: Net-(R83-Pad2) -> unconnected-(U10-IN-3-Pad1)
- U10 pad 2: Net-(U10A--) -> unconnected-(U10-IN+3-Pad2)
- U10 pad 3: Net-(U10A-+) -> GND
- U10 pad 4: GND -> +3.3V Boot
- U10 pad 5: Net-(U10B-+) -> GND
- U10 pad 6: Net-(U10B--) -> I²C SCL_0
- U10 pad 7: Net-(R84-Pad2) -> I²C SDA_0
- U10 pad 8: +3.3V Boot -> FAULT_WARNING_SUM
- U11 pad 1: Net-(D16-A) -> Incoming (-)
- U11 pad 2: Net-(U11A-IN-) -> Incoming (+)
- U11 pad 3: Net-(U11A-IN+) -> GND
- U11 pad 4: GND -> +3.3V Boot
- U11 pad 5: Net-(U11B-IN+) -> +3.3V Boot
- U11 pad 6: Net-(U11B-IN-) -> I²C SCL_0
- U11 pad 7: Net-(D16-A) -> I²C SDA_0
- U11 pad 8: +12V -> FAULT_WARNING_SUM
- U12 pad 1: Net-(D17-A) -> Net-(R80-Pad2)
- U12 pad 2: Net-(U12A-IN-) -> Net-(U12A--)
- U12 pad 3: Net-(U12A-IN+) -> Net-(U12A-+)
- U12 pad 5: Net-(U12B-IN+) -> Net-(U12B-+)
- U12 pad 6: Net-(U12B-IN-) -> Net-(U12B--)
- U12 pad 7: Net-(D17-A) -> Net-(R94-Pad2)
- U12 pad 8: +12V -> +3.3V Boot
- U13 pad 1: unconnected-(U13-IN-3-Pad1) -> Net-(D20-A)
- U13 pad 2: unconnected-(U13-IN+3-Pad2) -> Net-(U13A-IN-)
- U13 pad 3: GND -> Net-(U13A-IN+)
- U13 pad 4: +3.3V Boot -> GND
- U13 pad 5: GND -> Net-(U13B-IN+)
- U13 pad 6: I²C SCL_0 -> Net-(U13B-IN-)
- U13 pad 7: I²C SDA_0 -> Net-(D20-A)
- U13 pad 8: FAULT_WARNING_SUM -> +12V
- U14 pad 1: Incoming (-) -> ESP- GPIO 5V Low
- U14 pad 2: Incoming (+) -> GND
- U14 pad 3: GND -> unconnected-(U14-NC-Pad3)
- U14 pad 4: +3.3V Boot -> Net-(U14-VCAP)
- U14 pad 5: +3.3V Boot -> +5V_Boot
- U14 pad 6: I²C SCL_0 -> Net-(U14-GATE)
- U14 pad 7: I²C SDA_0 -> Net-(U14-OV)
- U14 pad 8: FAULT_WARNING_SUM -> SRC 5_LOW
- U2 pad 5: Net-(Q2-D) -> Net-(Q3-D)
- U3 pad 1: ESP- GPIO 5V Hi -> Net-(D8-A-Pad1)
- U3 pad 2: GND -> Net-(D8-A-Pad1)
- U3 pad 3: unconnected-(U3-NC-Pad3) -> VSENSE_3V3+
- U3 pad 4: Net-(U3-VCAP) -> GND
- U3 pad 5: +5V_Boot -> Net-(R28-Pad2)
- U3 pad 6: Net-(U3-GATE) -> Net-(D8-A-Pad2)
- U3 pad 7: Net-(U3-OV) -> Net-(D8-A-Pad2)
- U3 pad 8: SRC 5_HIGH -> +12V
- U4 pad 1: Net-(D6-A-Pad1) -> Net-(U4-VIN)
- U4 pad 2: Net-(D6-A-Pad1) -> Net-(U4-OUT)
- U4 pad 3: VSENSE_3V3+ -> GND
- U4 pad 4: GND -> Net-(U4-FB)
- U4 pad 5: Net-(R29-Pad2) -> Net-(Q12-D)
- U5 pad 1: Net-(D7-A-Pad1) -> Net-(U5-P1_0)
- U5 pad 2: Net-(D7-A-Pad1) -> unconnected-(U5-P1_1-Pad2)
- U5 pad 3: VSENSE_5V+ -> unconnected-(U5-P1_2-Pad3)
- U5 pad 4: GND -> unconnected-(U5-P1_3-Pad4)
- U5 pad 5: Net-(R35-Pad2) -> ISET_MPU_5V
- U5 pad 6: Net-(D7-A-Pad2) -> ESP- GPIO 5V Hi
- U5 pad 7: Net-(D7-A-Pad2) -> ESP- GPIO 5V Low
- U5 pad 8: +12V -> ESP- GPIO 3.3V High
- U6 pad 1: ESP- GPIO 5V Low -> Net-(R56-Pad2)
- U6 pad 2: GND -> Net-(U6A--)
- U6 pad 3: unconnected-(U6-NC-Pad3) -> Net-(U6A-+)
- U6 pad 4: Net-(U6-VCAP) -> GND
- U6 pad 5: +5V_Boot -> Net-(U6B-+)
- U6 pad 6: Net-(U6-GATE) -> Net-(U6B--)
- U6 pad 7: Net-(U6-OV) -> Net-(R74-Pad2)
- U6 pad 8: SRC 5_LOW -> +3.3V Boot
- U7 pad 1: ESP- GPIO 3.3V High -> Net-(D17-A)
- U7 pad 2: GND -> Net-(U7A-IN-)
- U7 pad 3: unconnected-(U7-NC-Pad3) -> Net-(U7A-IN+)
- U7 pad 4: Net-(U7-VCAP) -> GND
- U7 pad 5: +5V_Boot -> Net-(U7B-IN+)
- U7 pad 6: Net-(U7-GATE) -> Net-(U7B-IN-)
- U7 pad 7: Net-(U7-OV) -> Net-(D17-A)
- U7 pad 8: SRC 3.3_HIGH -> +12V
- U8 pad 1: ESP- GPIO 3.3V Low -> Net-(U8-VIN)
- U8 pad 2: GND -> Net-(U8-OUT)
- U8 pad 3: unconnected-(U8-NC-Pad3) -> GND
- U8 pad 4: Net-(U8-VCAP) -> Net-(U8-FB)
- U8 pad 5: +5V_Boot -> GND
- U9 pad 1: Net-(R81-Pad2) -> ESP- GPIO 5V Hi
- U9 pad 2: Net-(U9A--) -> GND
- U9 pad 3: Net-(U9A-+) -> unconnected-(U9-NC-Pad3)
- U9 pad 4: GND -> Net-(U9-VCAP)
- U9 pad 5: Net-(U9B-+) -> +5V_Boot
- U9 pad 6: Net-(U9B--) -> Net-(U9-GATE)
- U9 pad 7: Net-(R82-Pad2) -> Net-(U9-OV)
- U9 pad 8: +3.3V Boot -> SRC 5_HIGH
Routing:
- net +3.3V_Reg: track 19.8 -> 0.00 mm
- net SRC 3.3_LOW: track 18.4 -> 0.00 mm
- net SRC 3.3_HIGH: track 16.6 -> 0.00 mm
- net Net-(U2-OUT): track 16.5 -> 0.00 mm
- net Net-(U2-VIN): track 10.3 -> 0.00 mm
- net Net-(Q9-D): track 5.97 -> 0.00 mm
- net Net-(Q10-D): track 5.81 -> 0.00 mm
- net +12V: track 3.21 -> 0.00 mm
- removed copper zone on B.Cu, net GND
- removed copper zone on F.Cu, net GND
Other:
- board size 291.9 x 100.9 mm -> 100 x 125 mm
- board text removed: "True North Enterprise Solutions LLC"
